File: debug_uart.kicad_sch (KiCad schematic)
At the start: 7 parts, among them U1 NX1H35 PBGA625

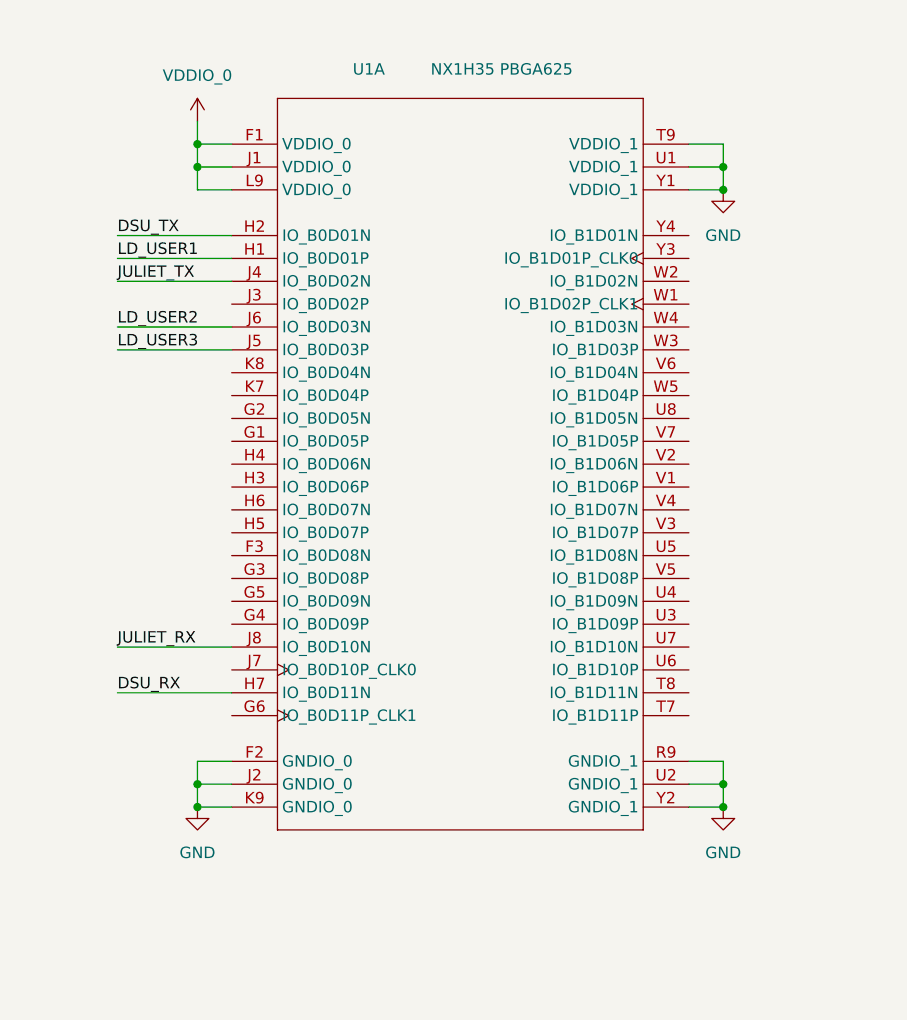
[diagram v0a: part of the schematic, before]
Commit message: SDRAM, bank5
last iteration of sdram. max optimization routing and space wise. Traced 2 frams to Bank 5. Fanout of bank 5 for DF9
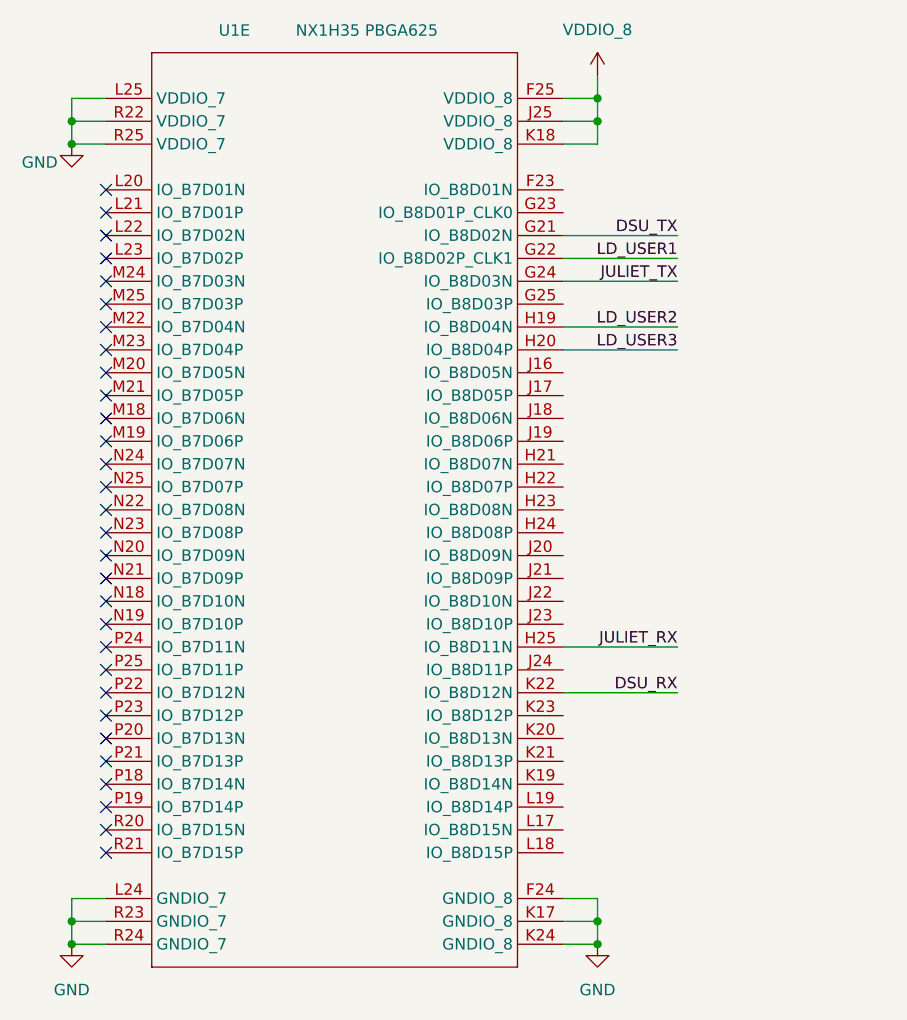
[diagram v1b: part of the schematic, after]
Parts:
- removed U1: NX1H35 PBGA625, DataHub_NG_Medium:NX1H35S_CLGA625, symbol Brave625:root_0_BRAVE625A_Brave625.SchLib
- added U1: NX1H35 PBGA625, DataHub_NG_Medium:NX1H35S_CLGA625, symbol Brave625:root_0_BRAVE625A_Brave625.SchLib
- R16, R17, R18: footprint Resistor_SMD:R_0603_1608Metric_Pad0.98x0.95mm_HandSolder -> Resistor_SMD:R_0402_1005Metric_Pad0.72x0.64mm_HandSolder
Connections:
- net DSU_RX: now also U1.K22 (IO_B8D12N)
- net DSU_TX: now also U1.G21 (IO_B8D02N)
- net GND: now also U1.F24 (GNDIO_8), U1.K17 (GNDIO_8), U1.K24 (GNDIO_8), U1.L24 (GNDIO_7), U1.L25 (VDDIO_7), U1.R22 (VDDIO_7), U1.R23 (GNDIO_7), U1.R24 (GNDIO_7), U1.R25 (VDDIO_7)
- net JULIET_RX: now also U1.H25 (IO_B8D11N)
- net JULIET_TX: now also U1.G24 (IO_B8D03N)
- net LD_USER1: now also U1.G22 (IO_B8D02P_CLK1)
- net LD_USER2: now also U1.H19 (IO_B8D04N)
- net LD_USER3: now also U1.H20 (IO_B8D04P)
- new net VDDIO_8: U1.F25 (VDDIO_8), U1.J25 (VDDIO_8), U1.K18 (VDDIO_8)
- no-connect marks 0 -> 30

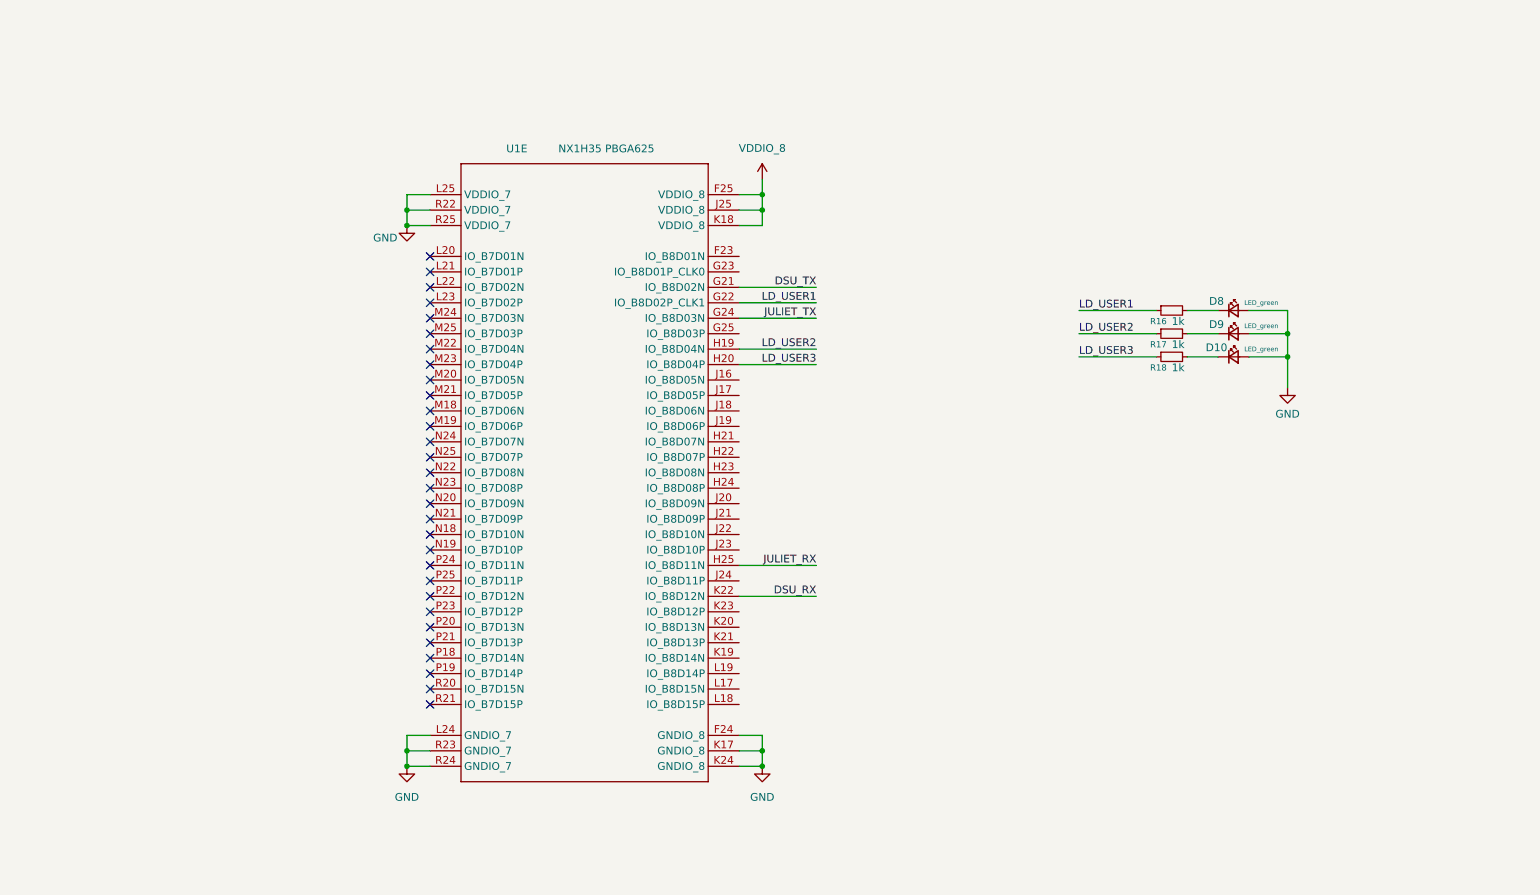
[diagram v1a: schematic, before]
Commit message: full components, LEDS, changed edges
all components on pcb editor. added and  routed leds and 2 PLL. changed edges o have more space
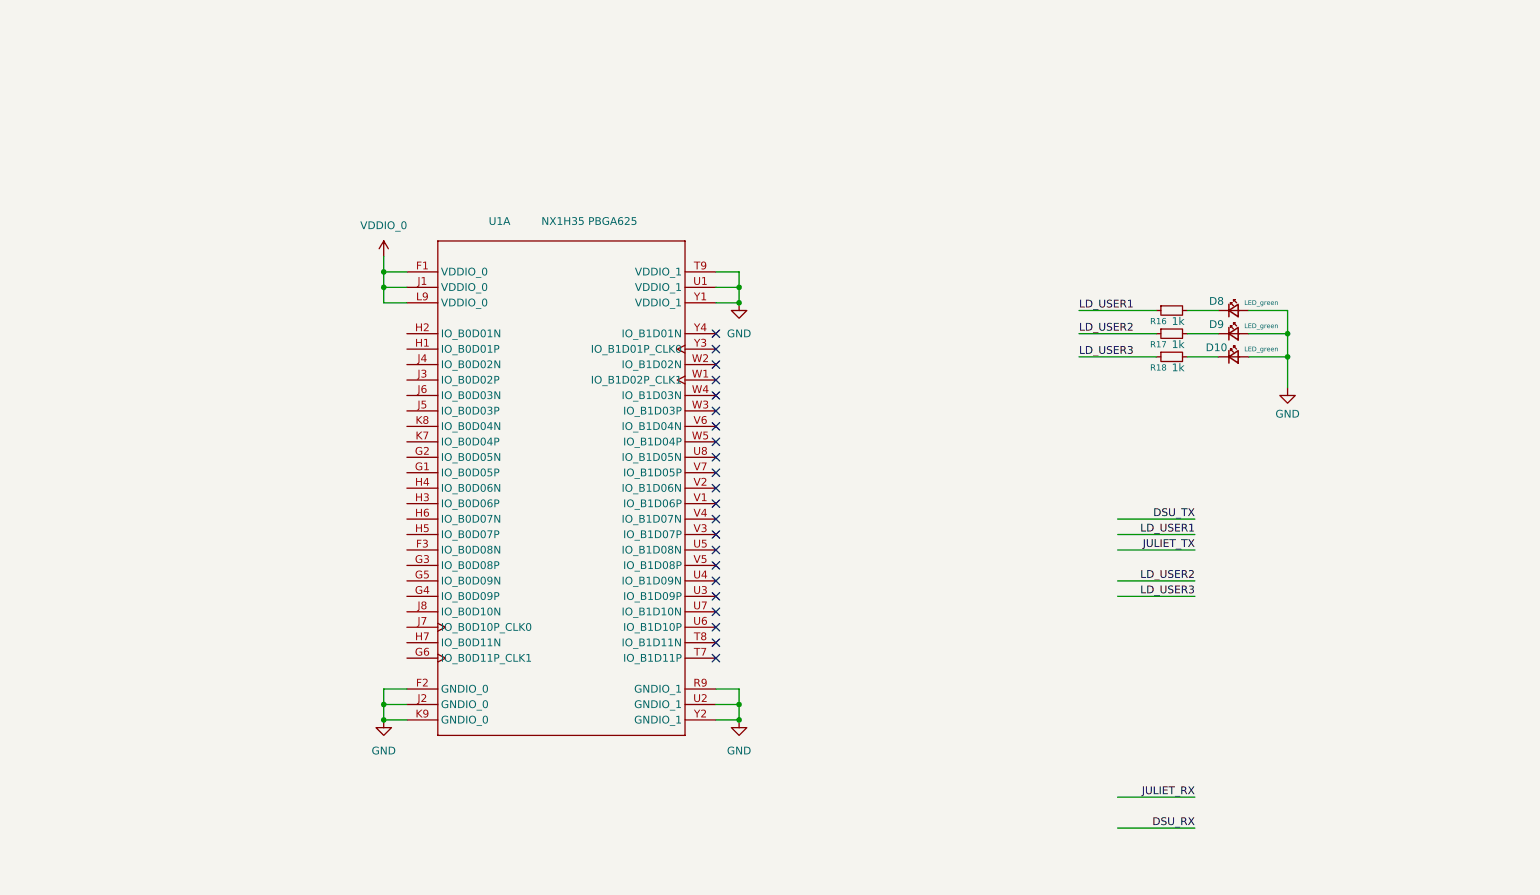
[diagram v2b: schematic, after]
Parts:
- removed U1: NX1H35 PBGA625, DataHub_NG_Medium:NX1H35S_CLGA625, symbol Brave625:root_0_BRAVE625A_Brave625.SchLib
- added U1: NX1H35 PBGA625, DataHub_NG_Medium:NX1H35S_CLGA625, symbol Brave625:root_0_BRAVE625A_Brave625.SchLib
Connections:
- net GND: now also U1.F2 (GNDIO_0), U1.J2 (GNDIO_0), U1.K9 (GNDIO_0), U1.R9 (GNDIO_1), U1.T9 (VDDIO_1), U1.U1 (VDDIO_1), U1.U2 (GNDIO_1), U1.Y1 (VDDIO_1), U1.Y2 (GNDIO_1)
- new net VDDIO_0: U1.F1 (VDDIO_0), U1.J1 (VDDIO_0), U1.L9 (VDDIO_0)
- no-connect marks 30 -> 22

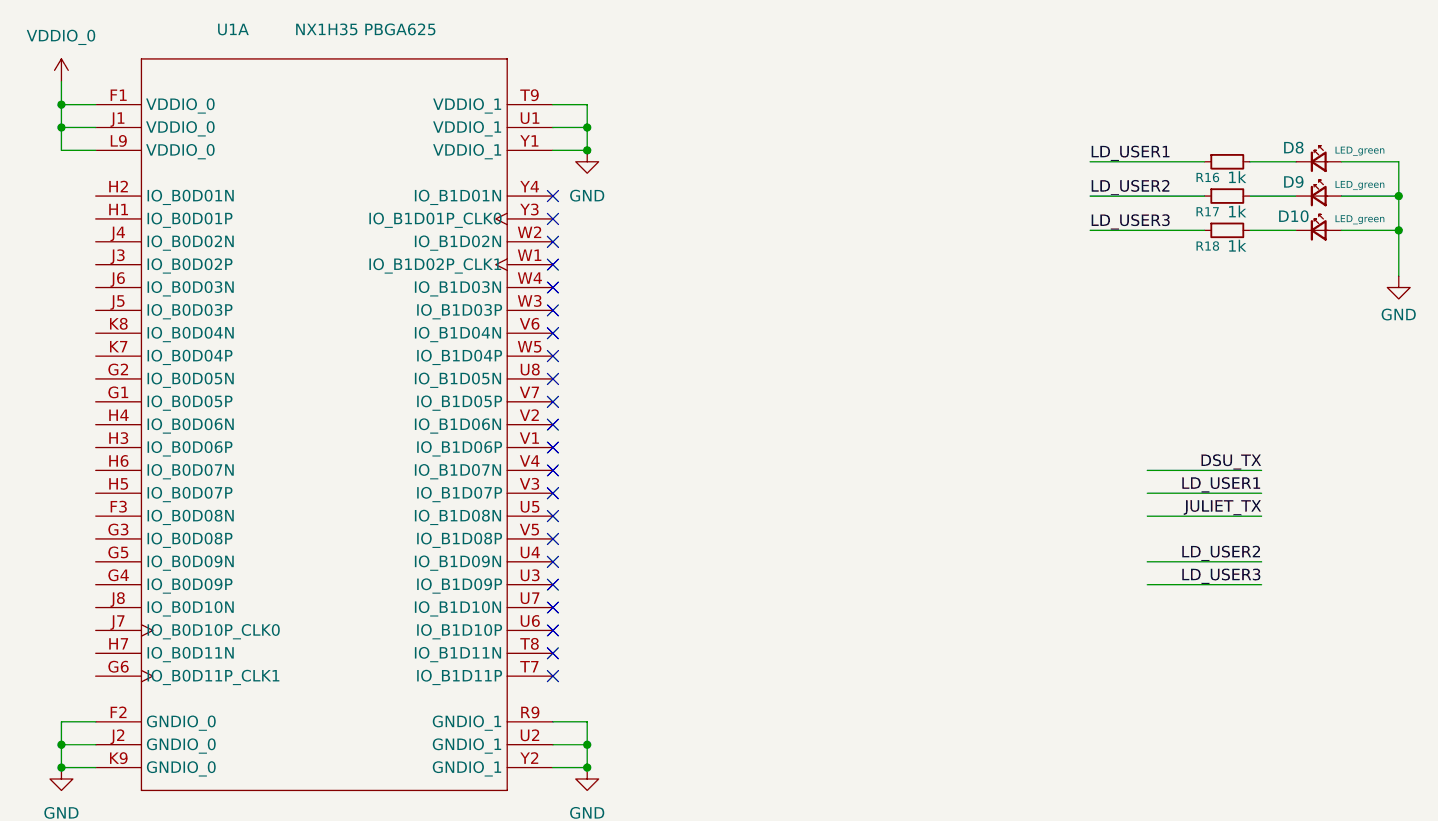
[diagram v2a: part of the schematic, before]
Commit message: CFG, bga sdram, banks to connectors, docoupling
Finished completely routing bga sdram, finished tracing Banks to connectors DF9. Finished tracing Picoblade, diode, reset supervisor. Finished tracing LEDS on bank 5. Finished decoupling all banks and core. Missing only the power tree and power rail level decoupling.
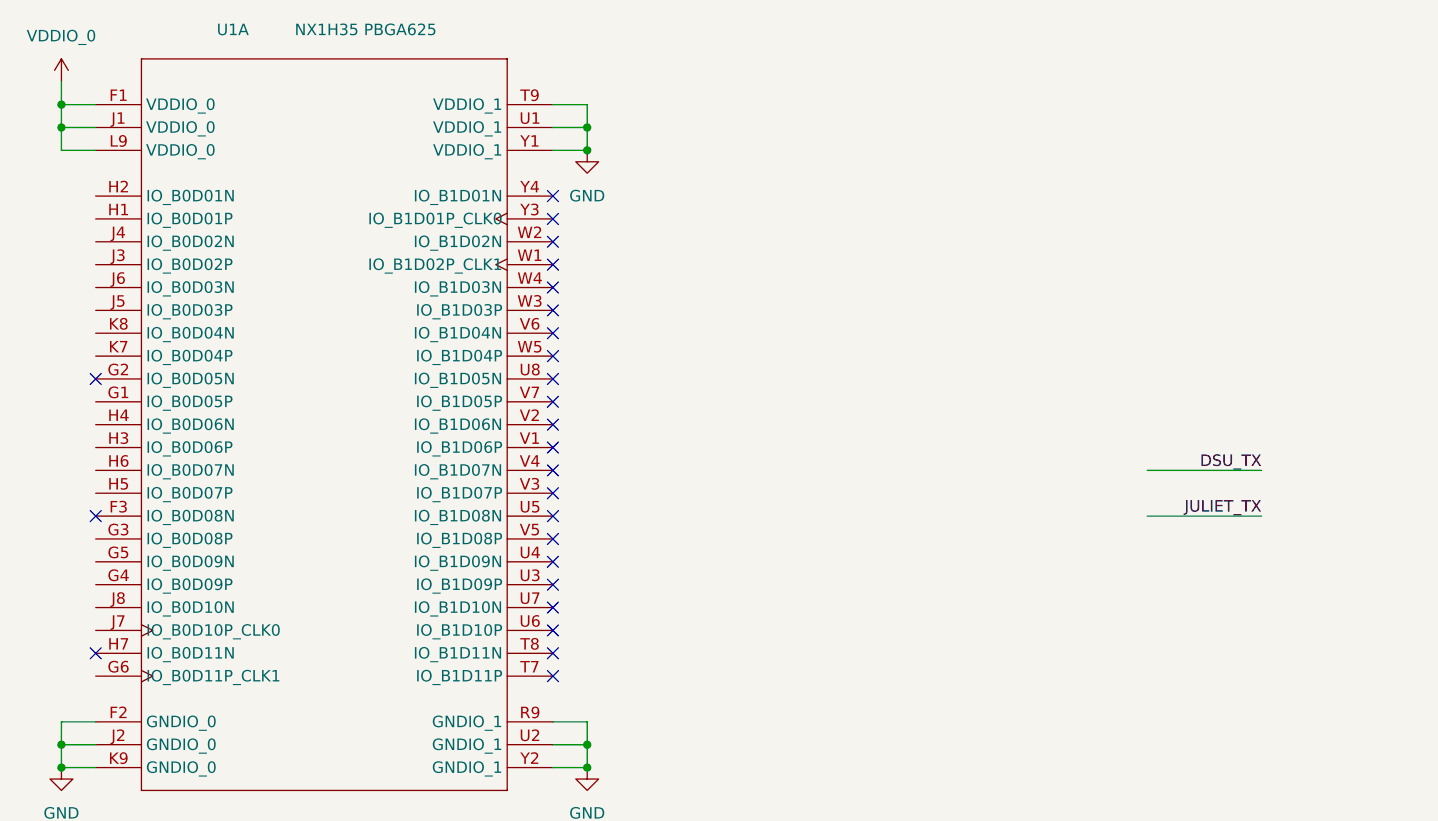
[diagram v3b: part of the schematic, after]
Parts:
- removed D10, D8, D9: LED_green, LED_SMD:LED_0603_1608Metric, symbol Device:LED_Small
- removed R16, R17, R18: 1k, Resistor_SMD:R_0402_1005Metric_Pad0.72x0.64mm_HandSolder, symbol Device:R_Small
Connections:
- no-connect marks 22 -> 25

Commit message: power tree
power tree defined. Few changes remaining but almost finalized
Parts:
- added unit 5 of U1
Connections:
- net GND: now also U1.F24 (GNDIO_8), U1.F25 (VDDIO_8), U1.J25 (VDDIO_8), U1.K17 (GNDIO_8), U1.K18 (VDDIO_8), U1.K24 (GNDIO_8), U1.L24 (GNDIO_7), U1.L25 (VDDIO_7), U1.R22 (VDDIO_7), U1.R23 (GNDIO_7), U1.R24 (GNDIO_7), U1.R25 (VDDIO_7)
- net B0_05P_DF9: now reaches U1.G1 (IO_B0D05P)
- net B0_08P_DF9: now reaches U1.G3 (IO_B0D08P)
- net B0_09P_DF9: now reaches U1.G4 (IO_B0D09P)
- net B0_09N_DF9: now reaches U1.G5 (IO_B0D09N)
- net B0_11P_DF9: now reaches U1.G6 (IO_B0D11P_CLK1)
- net B0_01P_DF9: now reaches U1.H1 (IO_B0D01P)
- net B0_01N_DF9: now reaches U1.H2 (IO_B0D01N)
- net B0_06P_DF9: now reaches U1.H3 (IO_B0D06P)
- net B0_06N_DF9: now reaches U1.H4 (IO_B0D06N)
- net B0_07P_DF9: now reaches U1.H5 (IO_B0D07P)
- net B0_07N_DF9: now reaches U1.H6 (IO_B0D07N)
- net B0_02P_DF9: now reaches U1.J3 (IO_B0D02P)
- net B0_02N_DF9: now reaches U1.J4 (IO_B0D02N)
- net B0_03P_DF9: now reaches U1.J5 (IO_B0D03P)
- net B0_03N_DF9: now reaches U1.J6 (IO_B0D03N)
- net B0_10P_DF9: now reaches U1.J7 (IO_B0D10P_CLK0)
- net B0_10N_DF9: now reaches U1.J8 (IO_B0D10N)
- net B0_04P_DF9: now reaches U1.K7 (IO_B0D04P)
- net B0_04N_DF9: now reaches U1.K8 (IO_B0D04N)
- no-connect marks 25 -> 85
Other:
- moved on the sheet: U1A

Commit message: finished
power planes, decoupling, ERC, DRC
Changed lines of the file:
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@@
 		(dnp no)
 		(property "Reference" "U1"
-			(at 197.612 40.1828 0)
+			(at 196.85 31.75 0)
 			(effects
 				(font
@@
 		)
 		(property "Value" "NX1H35 PBGA625"
-			(at 202.692 40.1828 0)
+			(at 201.93 31.75 0)
 			(effects
 				(font
@@
 					(unit 5)
 				)
+				(path "/ae14ff2f-b8e3-4dd1-9329-e73906805e39/77861c37-88e9-4408-9723-ec14cfd3d63b"
+					(reference "U1")
+					(unit 5)
+				)
 			)
 		)
@@
 	)
 	(symbol
+		(lib_name "root_0_BRAVE625A_Brave625.SchLib_1")
 		(lib_id "Brave625:root_0_BRAVE625A_Brave625.SchLib")
 		(at 90.17 85.09 0)
@@
 		(dnp no)
 		(property "Reference" "U1"
-			(at 81.788 47.0408 0)
+			(at 80.01 24.13 0)
 			(effects
 				(font
@@
 		)
 		(property "Value" "NX1H35 PBGA625"
-			(at 86.868 47.0408 0)
+			(at 85.09 24.13 0)
 			(effects
 				(font
@@
 					(reference "U1")
 					(unit 1)
+				)
+				(path "/ae14ff2f-b8e3-4dd1-9329-e73906805e39/77861c37-88e9-4408-9723-ec14cfd3d63b"
+					(reference "U1")
+					(unit 1)
